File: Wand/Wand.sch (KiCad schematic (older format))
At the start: 26 parts, among them IC1 ATMEGA328-MMH, J1 TIP, P1 ISP, P2 BASE, U1 OPA336U, U2 MPU-6050, Y1 16MHz

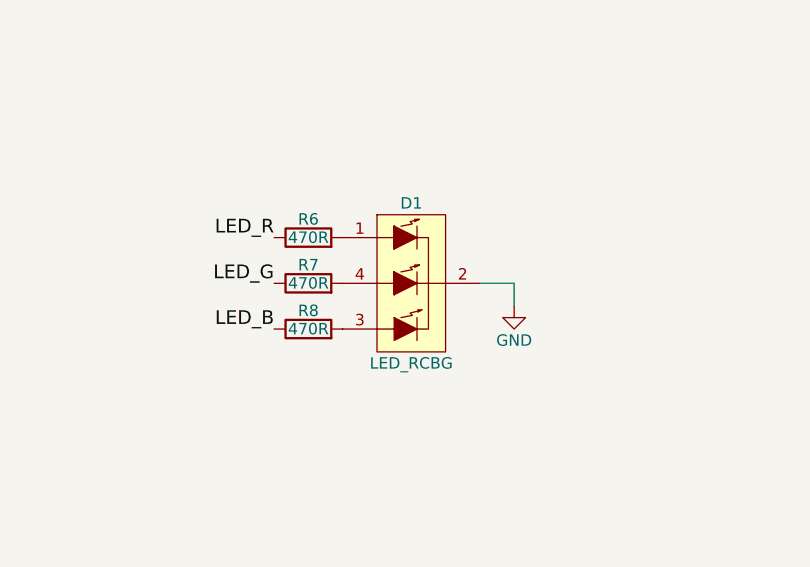
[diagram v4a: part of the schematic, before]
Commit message: Picked an RGB LED part and selected the correct resistor values
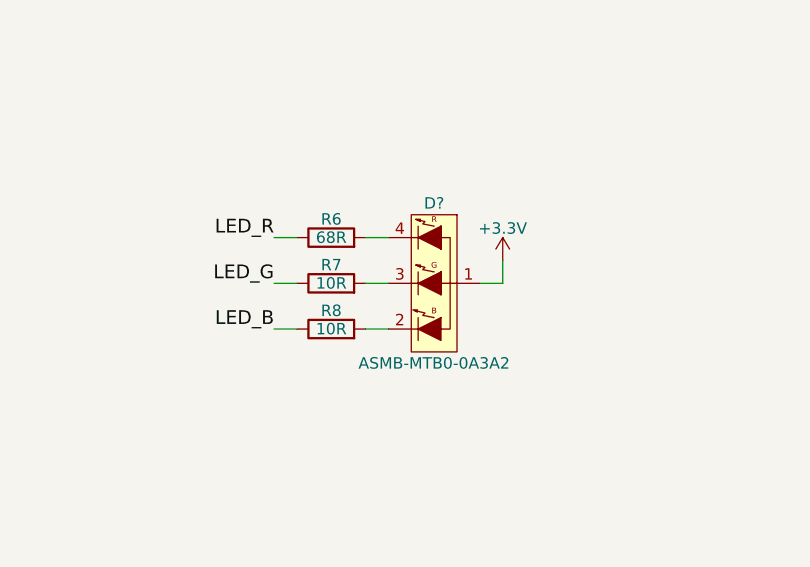
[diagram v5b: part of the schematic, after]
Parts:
- removed D1: LED_RCBG, symbol LED_RCBG
- added D?: ASMB-MTB0-0A3A2, symbol Led_BGR_CA
- R6: value 470R -> 68R
- R7, R8: value 470R -> 10R
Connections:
- net +3V3: now also D?.1
- net at R6.2: now also D?.4 (R)
- net at R8.2: now also D?.2 (B)
- net at R7.2: now also D?.3 (G)
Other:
- moved on the sheet: R6, R7, R8
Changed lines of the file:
@@
-$EndComp
-$Comp
-L LED_RCBG D1
-U 1 1 563E7860
-P 7350 4950
-F 0 "D1" H 7350 5300 50  0000 C CNN
-F 1 "LED_RCBG" H 7350 4600 50  0000 C CNN
-F 2 "" H 7350 4900 50  0000 C CNN
-F 3 "" H 7350 4900 50  0000 C CNN
-	1    7350 4950
-	-1   0    0    -1
 $EndComp
 $Comp
 L R R8
 U 1 1 563E78F7
-P 6900 5150
-F 0 "R8" V 6980 5150 50  0000 C CNN
-F 1 "470R" V 6900 5150 50  0000 C CNN
-F 2 "" V 6830 5150 30  0000 C CNN
-F 3 "" H 6900 5150 30  0000 C CNN
-	1    6900 5150
+P 7000 5150
+F 0 "R8" V 7080 5150 50  0000 C CNN
+F 1 "10R" V 7000 5150 50  0000 C CNN
+F 2 "" V 6930 5150 30  0000 C CNN
+F 3 "" H 7000 5150 30  0000 C CNN
+	1    7000 5150
 	0    -1   -1   0
 $EndComp
@@
 L R R7
 U 1 1 563E795E
-P 6900 4950
-F 0 "R7" V 6980 4950 50  0000 C CNN
-F 1 "470R" V 6900 4950 50  0000 C CNN
-F 2 "" V 6830 4950 30  0000 C CNN
-F 3 "" H 6900 4950 30  0000 C CNN
-	1    6900 4950
+P 7000 4950
+F 0 "R7" V 7080 4950 50  0000 C CNN
+F 1 "10R" V 7000 4950 50  0000 C CNN
+F 2 "" V 6930 4950 30  0000 C CNN
+F 3 "" H 7000 4950 30  0000 C CNN
+	1    7000 4950
 	0    -1   -1   0
 $EndComp
@@
 L R R6
 U 1 1 563E79E9
-P 6900 4750
-F 0 "R6" V 6980 4750 50  0000 C CNN
-F 1 "470R" V 6900 4750 50  0000 C CNN
-F 2 "" V 6830 4750 30  0000 C CNN
-F 3 "" H 6900 4750 30  0000 C CNN
-	1    6900 4750
+P 7000 4750
+F 0 "R6" V 7080 4750 50  0000 C CNN
+F 1 "68R" V 7000 4750 50  0000 C CNN
+F 2 "" V 6930 4750 30  0000 C CNN
+F 3 "" H 7000 4750 30  0000 C CNN
+	1    7000 4750
 	0    -1   -1   0
 $EndComp
@@
 	1    0    0    -1
 $EndComp
-$Comp
-L GND #PWR12
-U 1 1 5641471A
-P 7800 5050
-F 0 "#PWR12" H 7800 4800 50  0001 C CNN
-F 1 "GND" H 7800 4900 50  0000 C CNN
-F 2 "" H 7800 5050 60  0000 C CNN
-F 3 "" H 7800 5050 60  0000 C CNN
-	1    7800 5050
-	1    0    0    -1
-$EndComp
 Text Label 6750 4750 2    60   ~ 0
 LED_R
@@
 	4750 5750 4750 5800
 Connection ~ 4750 5750
-Wire Wire Line
-	7650 4950 7800 4950
-Wire Wire Line
-	7800 4950 7800 5050
 Wire Wire Line
 	3600 2100 3750 2100
@@
 Wire Wire Line
 	4700 3350 4700 3450
+Wire Wire Line
+	6750 4750 6850 4750
+Wire Wire Line
+	6750 4950 6850 4950
+Wire Wire Line
+	6750 5150 6850 5150
+Wire Wire Line
+	7150 5150 7250 5150
+Wire Wire Line
+	7150 4950 7250 4950
+Wire Wire Line
+	7150 4750 7250 4750
+$Comp
+L +3.3V #PWR?
+U 1 1 56483A48
+P 7750 4850
+F 0 "#PWR?" H 7750 4700 50  0001 C CNN
+F 1 "+3.3V" H 7750 4990 50  0000 C CNN
+F 2 "" H 7750 4850 60  0000 C CNN
+F 3 "" H 7750 4850 60  0000 C CNN
+	1    7750 4850
+	1    0    0    -1
+$EndComp
+Wire Wire Line
+	7650 4950 7750 4950
+Wire Wire Line
+	7750 4950 7750 4850
+$Comp
+L Led_BGR_CA D?
+U 1 1 56483D93
+P 7450 4950
+F 0 "D?" H 7450 5300 50  0000 C CNN
+F 1 "ASMB-MTB0-0A3A2" H 7450 4600 50  0000 C CNN
+F 2 "" H 7405 4900 50  0000 C CNN
+F 3 "" H 7405 4900 50  0000 C CNN
+	1    7450 4950
+	1    0    0    -1
+$EndComp
 $EndSCHEMATC

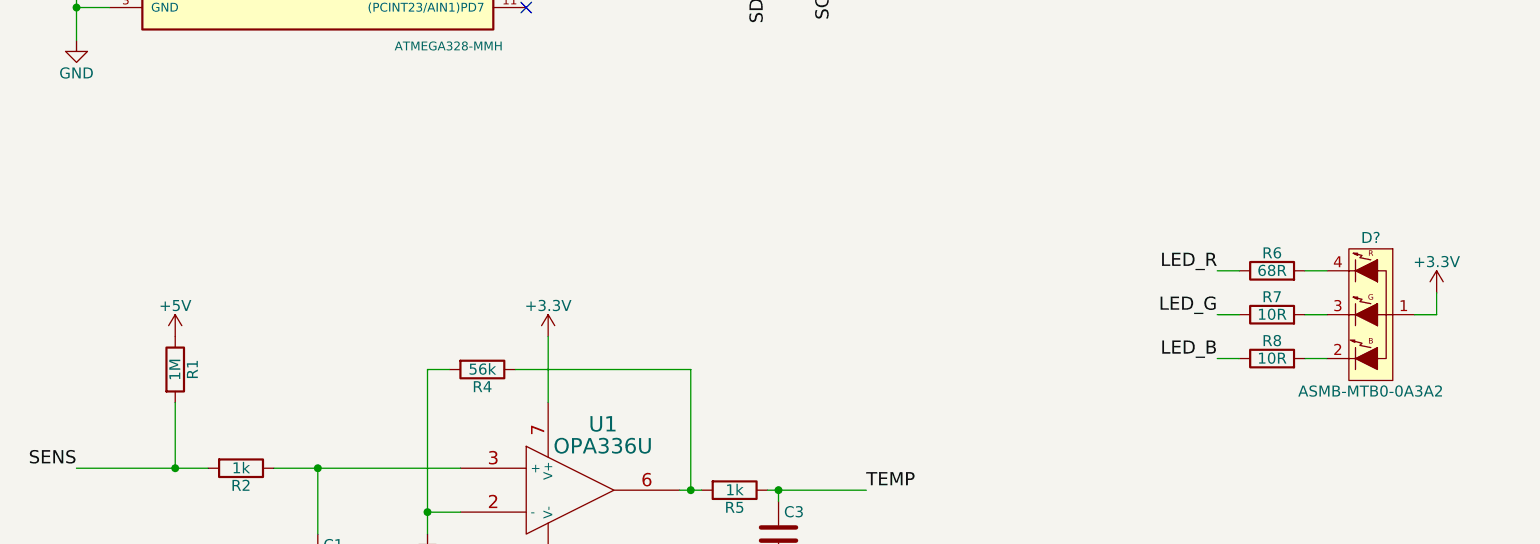
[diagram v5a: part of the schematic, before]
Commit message: Fixed a 5v that should be 3.3v
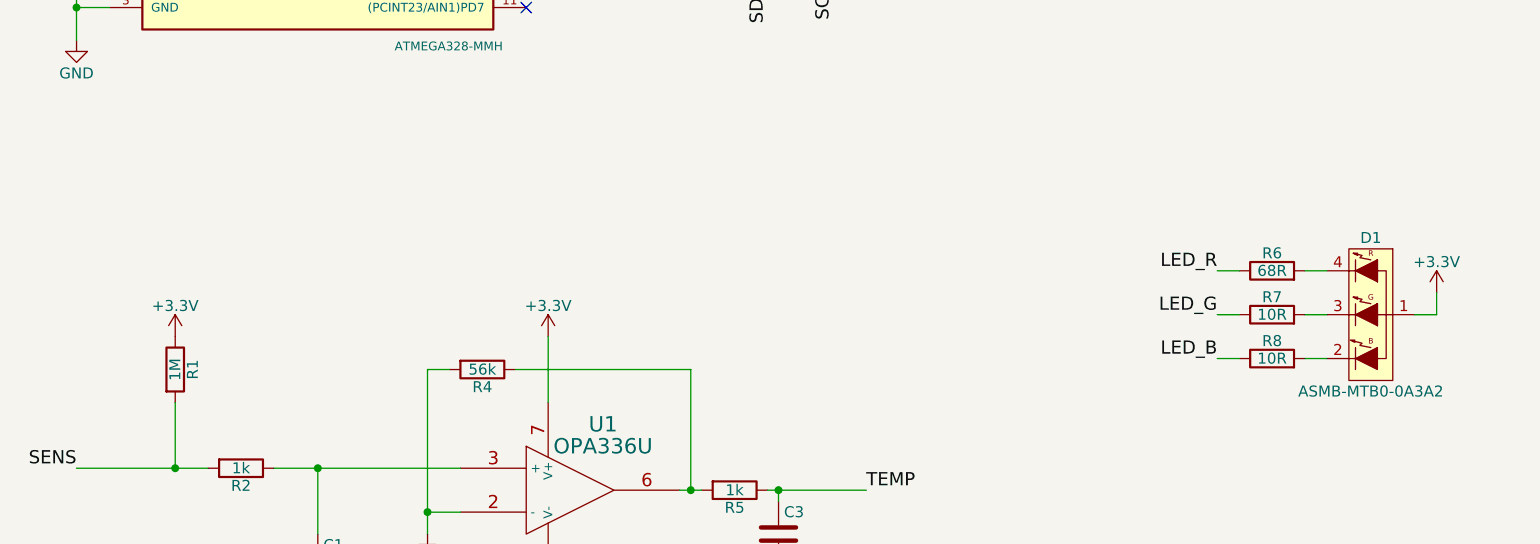
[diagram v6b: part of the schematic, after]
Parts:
- gave numbers to parts that had none: 1
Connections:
- net +5V is gone; now on net +3V3: R1.1
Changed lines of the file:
@@
 $EndComp
 $Comp
-L GND #PWR6
+L GND #PWR01
 U 1 1 5641252D
 P 3700 6450
-F 0 "#PWR6" H 3700 6200 50  0001 C CNN
+F 0 "#PWR01" H 3700 6200 50  0001 C CNN
 F 1 "GND" H 3700 6300 50  0000 C CNN
 F 2 "" H 3700 6450 60  0000 C CNN
@@
 SENS
 $Comp
-L GND #PWR4
+L GND #PWR02
 U 1 1 56412884
 P 2650 6450
-F 0 "#PWR4" H 2650 6200 50  0001 C CNN
+F 0 "#PWR02" H 2650 6200 50  0001 C CNN
 F 1 "GND" H 2650 6300 50  0000 C CNN
 F 2 "" H 2650 6450 60  0000 C CNN
@@
 $EndComp
 $Comp
-L GND #PWR7
+L GND #PWR03
 U 1 1 564128BC
 P 4750 6450
-F 0 "#PWR7" H 4750 6200 50  0001 C CNN
+F 0 "#PWR03" H 4750 6200 50  0001 C CNN
 F 1 "GND" H 4750 6300 50  0000 C CNN
 F 2 "" H 4750 6450 60  0000 C CNN
@@
 Text Label 5150 5750 0    60   ~ 0
 TEMP
-$Comp
-L +5V #PWR3
-U 1 1 564142EE
-P 2000 5050
-F 0 "#PWR3" H 2000 4900 50  0001 C CNN
-F 1 "+5V" H 2000 5190 50  0000 C CNN
-F 2 "" H 2000 5050 60  0000 C CNN
-F 3 "" H 2000 5050 60  0000 C CNN
-	1    2000 5050
-	1    0    0    -1
-$EndComp
 Text Label 6750 4750 2    60   ~ 0
 LED_R
@@
 TEMP
 $Comp
-L GND #PWR9
+L GND #PWR05
 U 1 1 56415081
 P 5000 2450
-F 0 "#PWR9" H 5000 2200 50  0001 C CNN
+F 0 "#PWR05" H 5000 2200 50  0001 C CNN
 F 1 "GND" H 5000 2300 50  0000 C CNN
 F 2 "" H 5000 2450 60  0000 C CNN
@@
 $EndComp
 $Comp
-L GND #PWR2
+L GND #PWR06
 U 1 1 56415406
 P 1550 3700
-F 0 "#PWR2" H 1550 3450 50  0001 C CNN
+F 0 "#PWR06" H 1550 3450 50  0001 C CNN
 F 1 "GND" H 1550 3550 50  0000 C CNN
 F 2 "" H 1550 3700 60  0000 C CNN
@@
 $EndComp
 $Comp
-L GND #PWR14
+L GND #PWR07
 U 1 1 56416557
 P 9400 5750
-F 0 "#PWR14" H 9400 5500 50  0001 C CNN
+F 0 "#PWR07" H 9400 5500 50  0001 C CNN
 F 1 "GND" H 9400 5600 50  0000 C CNN
 F 2 "" H 9400 5750 60  0000 C CNN
@@
 MOSI
 $Comp
-L GND #PWR18
+L GND #PWR08
 U 1 1 56417D51
 P 10300 4000
-F 0 "#PWR18" H 10300 3750 50  0001 C CNN
+F 0 "#PWR08" H 10300 3750 50  0001 C CNN
 F 1 "GND" H 10300 3850 50  0000 C CNN
 F 2 "" H 10300 4000 60  0000 C CNN
@@
 $EndComp
 $Comp
-L GND #PWR16
+L GND #PWR09
 U 1 1 56417FF2
 P 9900 2350
-F 0 "#PWR16" H 9900 2100 50  0001 C CNN
+F 0 "#PWR09" H 9900 2100 50  0001 C CNN
 F 1 "GND" H 9900 2200 50  0000 C CNN
 F 2 "" H 9900 2350 60  0000 C CNN
@@
 NoConn ~ 8700 2100
 $Comp
-L PWR_FLAG #FLG1
+L PWR_FLAG #FLG010
 U 1 1 5641AE63
 P 10000 1750
-F 0 "#FLG1" H 10000 1845 50  0001 C CNN
+F 0 "#FLG010" H 10000 1845 50  0001 C CNN
 F 1 "PWR_FLAG" H 10000 1930 50  0000 C CNN
 F 2 "" H 10000 1750 60  0000 C CNN
@@
 $EndComp
 $Comp
-L PWR_FLAG #FLG2
+L PWR_FLAG #FLG011
 U 1 1 5641AE9F
 P 10000 2550
-F 0 "#FLG2" H 10000 2645 50  0001 C CNN
+F 0 "#FLG011" H 10000 2645 50  0001 C CNN
 F 1 "PWR_FLAG" H 10000 2730 50  0000 C CNN
 F 2 "" H 10000 2550 60  0000 C CNN
@@
 	10300 3950 10300 4000
 $Comp
-L +3.3V #PWR15
+L +3.3V #PWR012
 U 1 1 5647AD9A
 P 9900 1950
-F 0 "#PWR15" H 9900 1800 50  0001 C CNN
+F 0 "#PWR012" H 9900 1800 50  0001 C CNN
 F 1 "+3.3V" H 9900 2090 50  0000 C CNN
 F 2 "" H 9900 1950 60  0000 C CNN
@@
 $EndComp
 $Comp
-L +3.3V #PWR11
+L +3.3V #PWR013
 U 1 1 5647B486
 P 7000 1450
-F 0 "#PWR11" H 7000 1300 50  0001 C CNN
+F 0 "#PWR013" H 7000 1300 50  0001 C CNN
 F 1 "+3.3V" H 7000 1590 50  0000 C CNN
 F 2 "" H 7000 1450 60  0000 C CNN
@@
 $EndComp
 $Comp
-L +3.3V #PWR1
+L +3.3V #PWR014
 U 1 1 5647BAD5
 P 1450 1200
-F 0 "#PWR1" H 1450 1050 50  0001 C CNN
+F 0 "#PWR014" H 1450 1050 50  0001 C CNN
 F 1 "+3.3V" H 1450 1340 50  0000 C CNN
 F 2 "" H 1450 1200 60  0000 C CNN
@@
 $EndComp
 $Comp
-L +3.3V #PWR5
+L +3.3V #PWR015
 U 1 1 5647C7BA
 P 3700 5050
-F 0 "#PWR5" H 3700 4900 50  0001 C CNN
+F 0 "#PWR015" H 3700 4900 50  0001 C CNN
 F 1 "+3.3V" H 3700 5190 50  0000 C CNN
 F 2 "" H 3700 5050 60  0000 C CNN
@@
 $EndComp
 $Comp
-L +3.3V #PWR17
+L +3.3V #PWR016
 U 1 1 5647DBFE
 P 10300 3700
-F 0 "#PWR17" H 10300 3550 50  0001 C CNN
+F 0 "#PWR016" H 10300 3550 50  0001 C CNN
 F 1 "+3.3V" H 10300 3840 50  0000 C CNN
 F 2 "" H 10300 3700 60  0000 C CNN
@@
 $EndComp
 $Comp
-L GND #PWR10
+L GND #PWR017
 U 1 1 5647F13E
 P 6100 2400
-F 0 "#PWR10" H 6100 2150 50  0001 C CNN
+F 0 "#PWR017" H 6100 2150 50  0001 C CNN
 F 1 "GND" H 6100 2250 50  0000 C CNN
 F 2 "" H 6100 2400 60  0000 C CNN
@@
 $EndComp
 $Comp
-L GND #PWR13
+L GND #PWR018
 U 1 1 5647F1D7
 P 8900 2550
-F 0 "#PWR13" H 8900 2300 50  0001 C CNN
+F 0 "#PWR018" H 8900 2300 50  0001 C CNN
 F 1 "GND" H 8900 2400 50  0000 C CNN
 F 2 "" H 8900 2550 60  0000 C CNN
@@
 $EndComp
 $Comp
-L +3.3V #PWR8
+L +3.3V #PWR019
 U 1 1 56482043
 P 4850 2900
-F 0 "#PWR8" H 4850 2750 50  0001 C CNN
+F 0 "#PWR019" H 4850 2750 50  0001 C CNN
 F 1 "+3.3V" H 4850 3040 50  0000 C CNN
 F 2 "" H 4850 2900 60  0000 C CNN
@@
 	7150 4750 7250 4750
 $Comp
-L +3.3V #PWR?
+L +3.3V #PWR020
 U 1 1 56483A48
 P 7750 4850
-F 0 "#PWR?" H 7750 4700 50  0001 C CNN
+F 0 "#PWR020" H 7750 4700 50  0001 C CNN
 F 1 "+3.3V" H 7750 4990 50  0000 C CNN
 F 2 "" H 7750 4850 60  0000 C CNN
@@
 	7750 4950 7750 4850
 $Comp
-L Led_BGR_CA D?
+L Led_BGR_CA D1
 U 1 1 56483D93
 P 7450 4950
-F 0 "D?" H 7450 5300 50  0000 C CNN
+F 0 "D1" H 7450 5300 50  0000 C CNN
 F 1 "ASMB-MTB0-0A3A2" H 7450 4600 50  0000 C CNN
 F 2 "" H 7405 4900 50  0000 C CNN
@@
 	1    0    0    -1
 $EndComp
+$Comp
+L +3.3V #PWR?
+U 1 1 56485537
+P 2000 5050
+F 0 "#PWR?" H 2000 4900 50  0001 C CNN
+F 1 "+3.3V" H 2000 5190 50  0000 C CNN
+F 2 "" H 2000 5050 60  0000 C CNN
+F 3 "" H 2000 5050 60  0000 C CNN
+	1    2000 5050
+	1    0    0    -1
+$EndComp

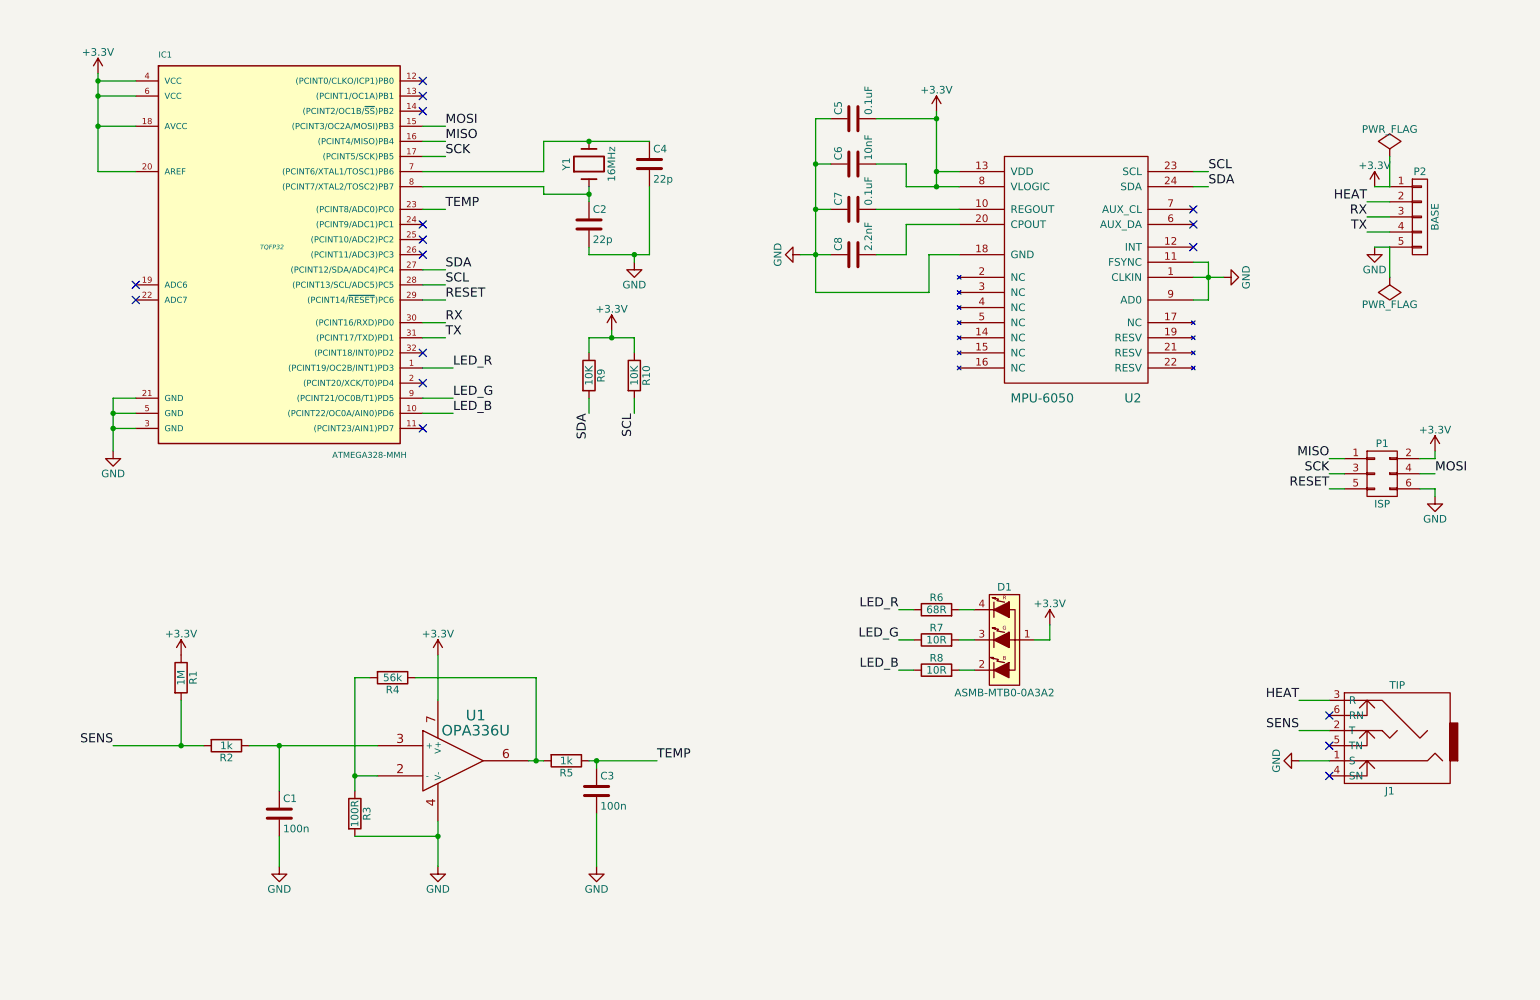
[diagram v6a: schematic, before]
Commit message: Added logic to detect the tip being inserted
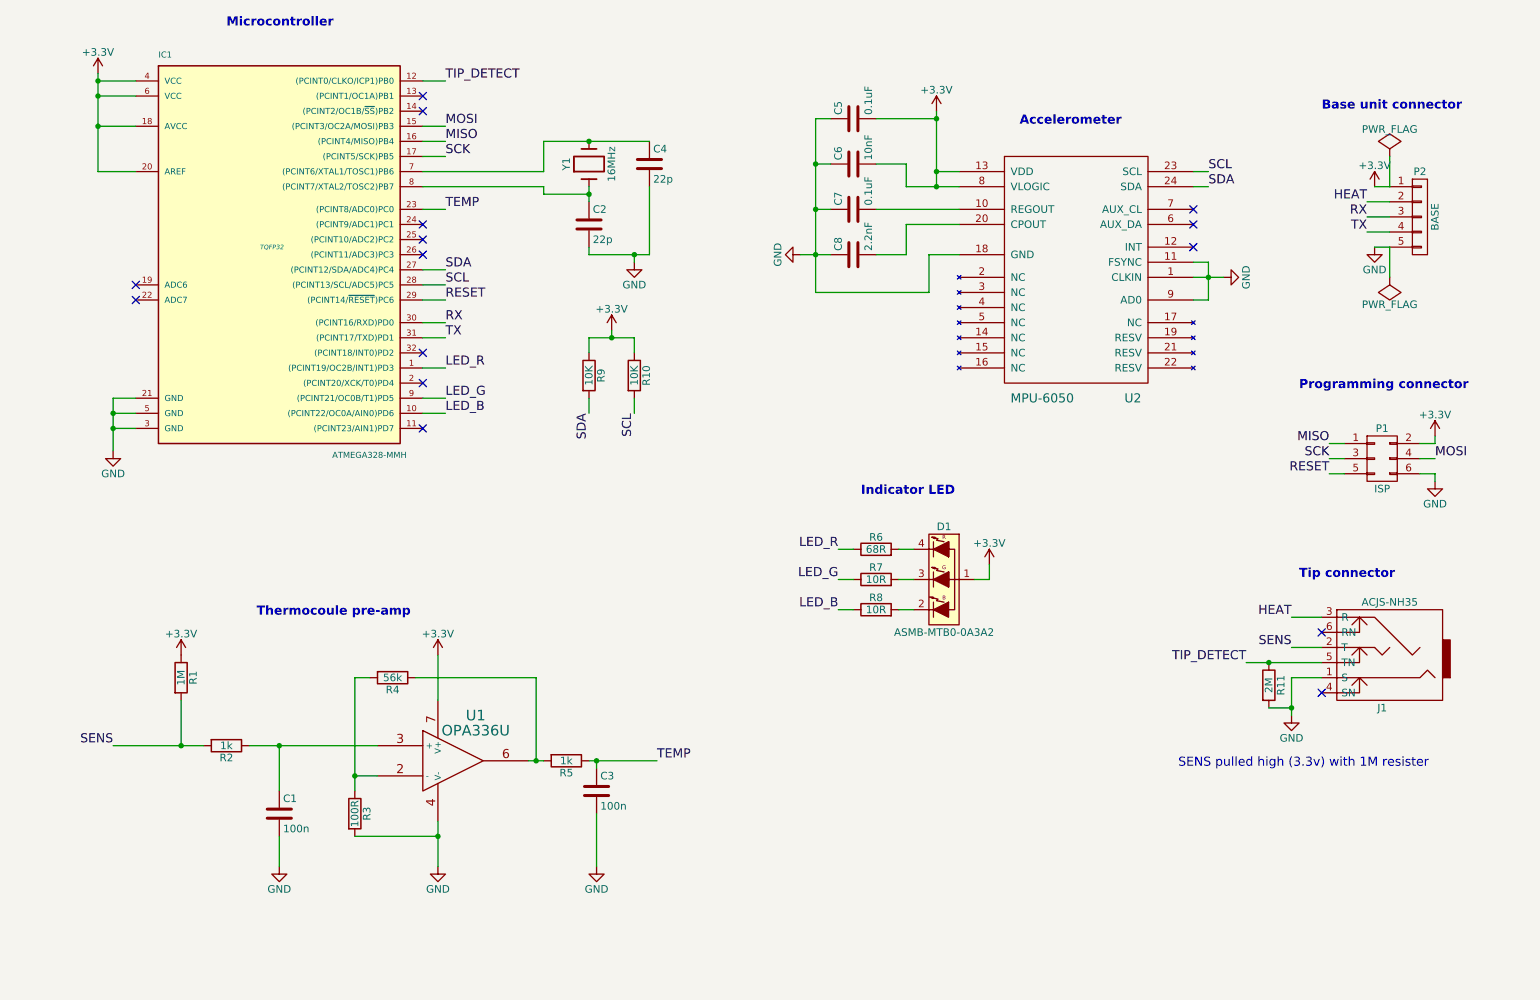
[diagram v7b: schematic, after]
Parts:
- added R11: 2M, symbol R
- J1: value TIP -> ACJS-NH35
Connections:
- net GND: now also R11.2
- net TIP_DETECT: now reaches IC1.12 ((PCINT0/CLKO/ICP1)PB0)
- net TIP_DETECT: now also J1.5 (TN), R11.1
- no-connect marks 17 -> 15
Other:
- note added: "Accelerometer"
- note added: "Base unit connector"
- note added: "Indicator LED"
- note added: "Microcontroller"
- note added: "Programming connector"
- note added: "SENS pulled high (3.3v) with 1M resister"
- note added: "Thermocoule pre-amp"
- note added: "Tip connector"
- moved on the sheet: D1, J1, P1, R6, R7, R8
